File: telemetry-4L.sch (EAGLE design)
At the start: 74 parts, among them SW1 MF-SW-TACT-4.2MM, SW2 PCM12SMTR, U1 ATSAMD21G18A-MUT, U2 SPX3819M5-L-3-0, U3 MCP73831T-2ACI/OT, U4 IRLML6344TRPBF, U5 SIM868, U6 BMP280, U7 MPU-9250, U8 TPS61253YFFR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

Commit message: More fixes of overlapping components
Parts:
- X4: MPN (none) -> 104239-1430
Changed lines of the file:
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@@
 <part name="X5" library="Seeed-Connector -2016" deviceset="ANTENNA-CONN-U-FL(3P)" device="" value="U.FL-R-SMT(10)"/>
 <part name="U$9" library="MF_Aesthetics" deviceset="GND_RAIL" device=""/>
-<part name="X4" library="SimSdCombo" deviceset="MOLEX-SD+SIM-104239" device="" value="104239-1430"/>
+<part name="X4" library="SimSdCombo" deviceset="MOLEX-SD+SIM-104239" device="" value="104239-1430">
+<attribute name="MPN" value="104239-1430"/>
+</part>
 <part name="U$4" library="microbuilder" deviceset="GND" device=""/>
 <part name="+3V11" library="MF_Aesthetics" deviceset="POWER_RAIL" device="" value="3V"/>

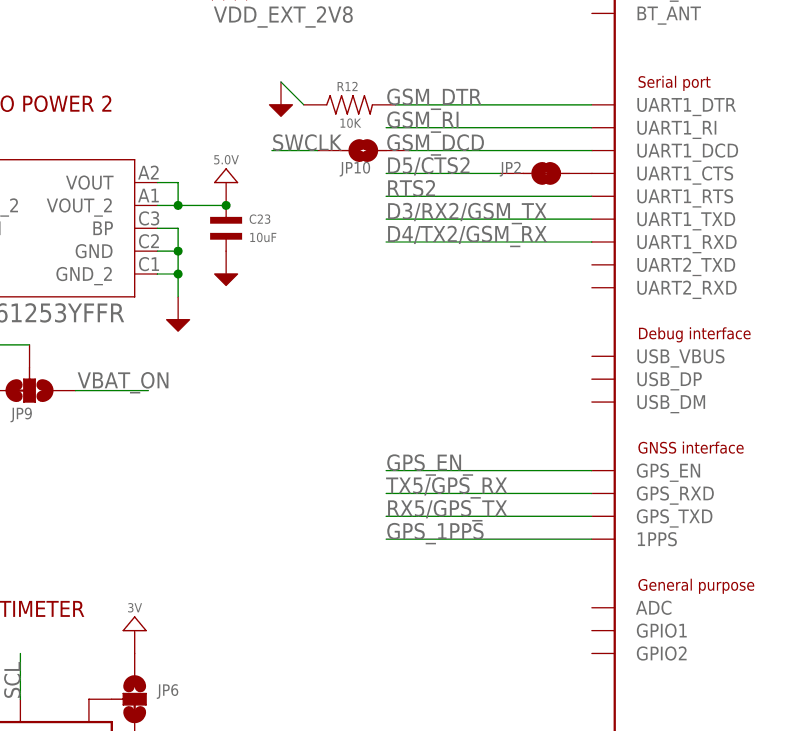
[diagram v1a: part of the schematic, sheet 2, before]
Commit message: Connected 1PPS via jumper made CTS jumper default NO
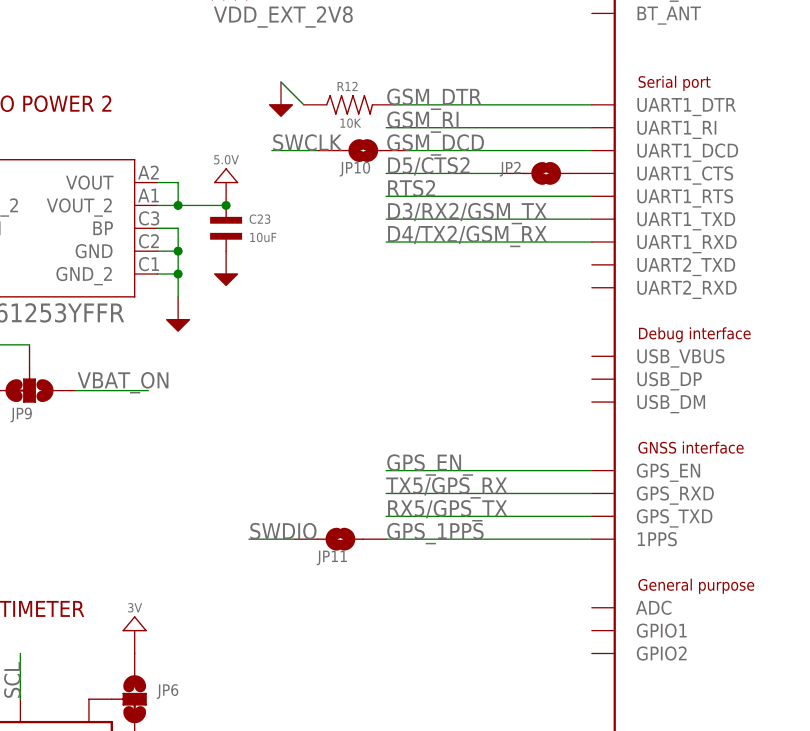
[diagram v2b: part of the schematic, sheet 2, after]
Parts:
- added JP11: JUMPER-PAD-2-NOYES_SILK, SparkFun-Passives:JUMPER-PAD-2-NOYES_SILK
- JP2: value JUMPER-PAD-2-NC_BY_TRACE -> JUMPER-PAD-2-NOYES_SILK; device SparkFun-Passives:JUMPER-PAD-2-NC_BY_TRACE -> SparkFun-Passives:JUMPER-PAD-2-NOYES_SILK
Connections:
- net GPS_1PPS: now also JP11.2
- net SWDIO: now also JP11.1
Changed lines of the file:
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@@
 <part name="U$43" library="MF_Aesthetics" deviceset="GND_RAIL" device=""/>
 <part name="U$48" library="microbuilder" deviceset="GND" device=""/>
-<part name="JP2" library="SparkFun-Passives" deviceset="JUMPER-PAD-2-NC_BY_TRACE" device="">
+<part name="JP2" library="SparkFun-Passives" deviceset="JUMPER-PAD-2-NO" device="YES_SILK">
 <attribute name="POPULATE" value="0"/>
 </part>
@@
 <part name="U$61" library="MF_Aesthetics" deviceset="GND_RAIL" device=""/>
 <part name="JP10" library="SparkFun-Passives" deviceset="JUMPER-PAD-2-NO" device="YES_SILK">
+<attribute name="POPULATE" value="0"/>
+</part>
+<part name="JP11" library="SparkFun-Passives" deviceset="JUMPER-PAD-2-NO" device="YES_SILK">
 <attribute name="POPULATE" value="0"/>
 </part>
@@
 <attribute name="NAME" x="137.16" y="114.3" size="1.27" layer="95"/>
 <attribute name="POPULATE" x="139.7" y="116.84" size="1.778" layer="96" display="off"/>
+</instance>
+<instance part="JP11" gate="G$1" x="137.16" y="73.66" smashed="yes">
+<attribute name="NAME" x="134.62" y="71.12" size="1.27" layer="95"/>
+<attribute name="POPULATE" x="137.16" y="73.66" size="1.778" layer="96" display="off"/>
 </instance>
 </instances>
@@
 <wire x1="165.1" y1="73.66" x2="142.24" y2="73.66" width="0.1524" layer="91"/>
 <label x="142.24" y="73.66" size="1.778" layer="95"/>
+<pinref part="JP11" gate="G$1" pin="2"/>
 </segment>
 </net>
@@
 </segment>
 </net>
+<net name="SWDIO" class="0">
+<segment>
+<pinref part="JP11" gate="G$1" pin="1"/>
+<wire x1="132.08" y1="73.66" x2="127" y2="73.66" width="0.1524" layer="91"/>
+<label x="127" y="73.66" size="1.778" layer="95"/>
+</segment>
+</net>

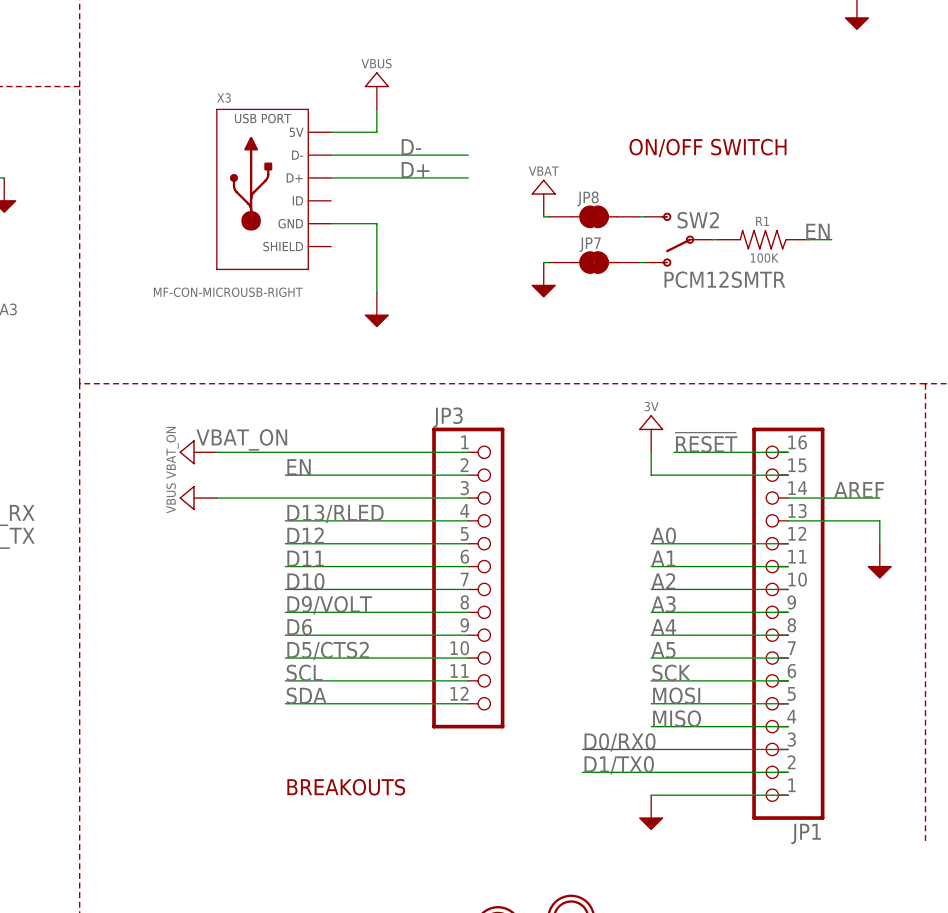
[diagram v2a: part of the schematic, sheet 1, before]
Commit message: Increased margins in middle part of board
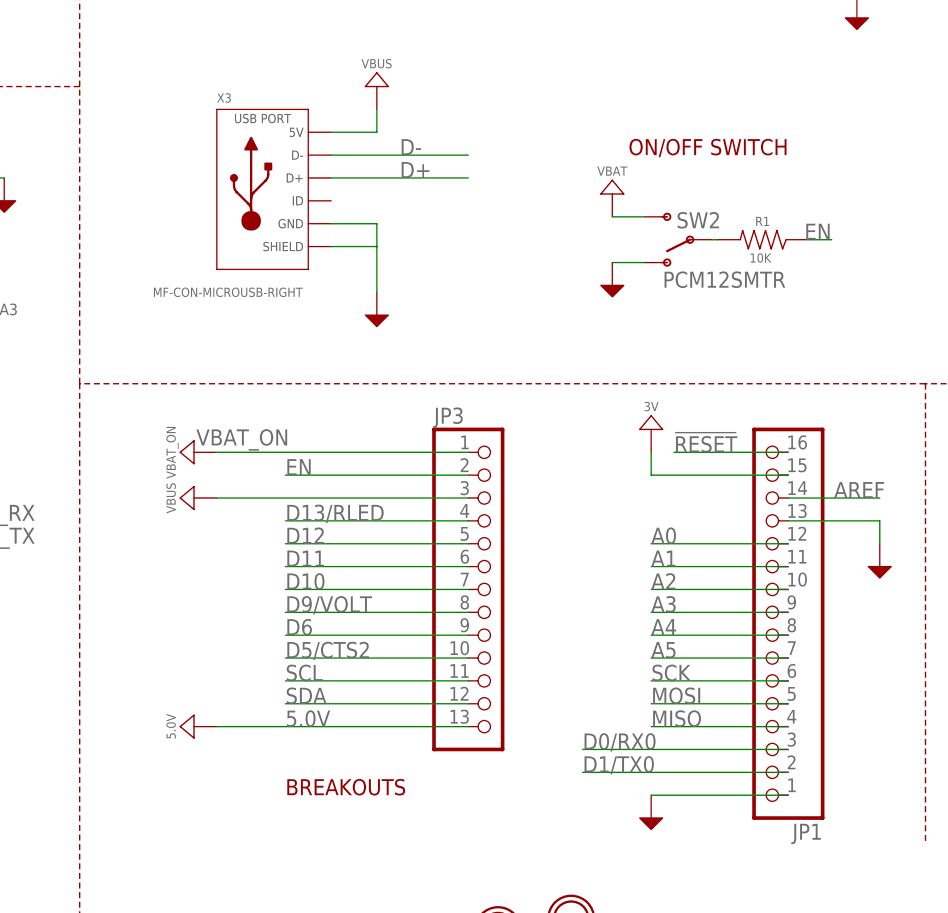
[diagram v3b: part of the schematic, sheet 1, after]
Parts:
- removed JP7, JP8: JUMPER-PAD-2-NC_BY_TRACE, SparkFun-Passives:JUMPER-PAD-2-NC_BY_TRACE
- removed X7: S2B-PH-SM4-TB(LF)(SN), microbuilder:CON_JST_PH_2PIN
- JP3: device microbuilder:HEADER-1X12 -> microbuilder:HEADER-1X13; POPULATE 0 -> (none)
- R1: value 100K -> 10K
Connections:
- removed net N$12: JP7.2, SW2.O
- removed net N$13: JP8.2, SW2.S
- net 5.0V: now also JP3.13; no longer X7.2
- net GND: now also SW2.O, X3.SLD; no longer JP7.1, X7.1
- net VBAT: now also SW2.S; no longer JP8.1
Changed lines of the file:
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@@
 <part name="U$16" library="MF_Aesthetics" deviceset="POWER_RAIL" device="" value="VBAT"/>
 <part name="U$22" library="MF_Aesthetics" deviceset="GND_RAIL" device=""/>
-<part name="JP3" library="microbuilder" deviceset="HEADER-1X12" device="">
-<attribute name="POPULATE" value="0"/>
-</part>
 <part name="U3" library="microbuilder" deviceset="MCP73831/2" device="" value="MCP73831T-2ACI/OT"/>
 <part name="U$33" library="MF_Aesthetics" deviceset="GND_RAIL" device=""/>
@@
 <part name="R8" library="MF_Passives" deviceset="RESISTOR" device="_0402" value="10K"/>
 <part name="R7" library="MF_Passives" deviceset="RESISTOR" device="_0402" value="1K"/>
-<part name="R1" library="MF_Passives" deviceset="RESISTOR" device="_0402" value="100K"/>
+<part name="R1" library="MF_Passives" deviceset="RESISTOR" device="_0402" value="10K"/>
 <part name="C1" library="MF_Passives" deviceset="CAPACITOR_NP" device="_0402" value="1uF"/>
 <part name="R4" library="MF_Passives" deviceset="RESISTOR" device="_0402" value="4.7K"/>
@@
 <part name="U$51" library="MF_Aesthetics" deviceset="GND_RAIL" device=""/>
 <part name="U$44" library="MF_Aesthetics" deviceset="POWER_RAIL" device="" value="VBAT"/>
-<part name="JP7" library="SparkFun-Passives" deviceset="JUMPER-PAD-2-NC_BY_TRACE" device="">
-<attribute name="POPULATE" value="0"/>
-</part>
-<part name="JP8" library="SparkFun-Passives" deviceset="JUMPER-PAD-2-NC_BY_TRACE" device="">
-<attribute name="POPULATE" value="0"/>
-</part>
 <part name="U4" library="MF_Discrete_Semiconductor" deviceset="N-CHANNEL_FET" device="_SOT-23-3" value="IRLML6344TRPBF"/>
 <part name="VBAT" library="MF_Aesthetics" deviceset="POWER_RAIL" device="" value="VBAT"/>
@@
 <part name="U$25" library="MF_Aesthetics" deviceset="GND_RAIL" device=""/>
 <part name="U$26" library="microbuilder" deviceset="GND" device=""/>
-<part name="X7" library="microbuilder" deviceset="CON_JST_PH_2PIN" device="" value="S2B-PH-SM4-TB(LF)(SN)"/>
 <part name="U8" library="Custom" deviceset="TPS61253YFFT" device="" value="TPS61253YFFR"/>
 <part name="L1" library="MF_Passives" deviceset="INDUCTOR" device="_1210" value="1uH">
@@
 <attribute name="POPULATE" value="0"/>
 </part>
+<part name="JP3" library="microbuilder" deviceset="HEADER-1X13" device=""/>
+<part name="5.0V" library="MF_Aesthetics" deviceset="POWER_RAIL" device="" value="5.0V"/>
 </parts>
 <sheets>
@@
 <attribute name="POPULATE" x="0" y="0" size="1.778" layer="96" display="off"/>
 </instance>
-<instance part="JP3" gate="G$1" x="180.34" y="66.04">
-<attribute name="POPULATE" x="180.34" y="66.04" size="1.778" layer="96" display="off"/>
-</instance>
 <instance part="U3" gate="G$1" x="187.96" y="144.78"/>
 <instance part="U$33" gate="G$1" x="220.98" y="129.54"/>
@@
 <instance part="U$45" gate="G$1" x="83.82" y="127"/>
 <instance part="U$47" gate="G$1" x="121.666" y="134.62"/>
-<instance part="U$49" gate="G$1" x="186.182" y="99.822"/>
+<instance part="U$49" gate="G$1" x="193.802" y="99.822"/>
 <instance part="U$50" gate="G$1" x="242.824" y="45.72"/>
 <instance part="U$51" gate="G$1" x="198.12" y="40.64"/>
-<instance part="U$44" gate="G$1" x="186.182" y="109.982"/>
-<instance part="JP7" gate="G$1" x="191.77" y="102.362" smashed="yes">
-<attribute name="NAME" x="190.246" y="103.886" size="1.27" layer="95"/>
-<attribute name="POPULATE" x="191.77" y="102.362" size="1.778" layer="96" display="off"/>
-</instance>
-<instance part="JP8" gate="G$1" x="191.77" y="107.442" smashed="yes">
-<attribute name="NAME" x="189.992" y="108.966" size="1.27" layer="95"/>
-<attribute name="POPULATE" x="191.77" y="107.442" size="1.778" layer="96" display="off"/>
-</instance>
+<instance part="U$44" gate="G$1" x="193.802" y="109.982"/>
 <instance part="U$59" gate="G$1" x="246.38" y="126.492"/>
 <instance part="U$60" gate="G$1" x="147.32" y="81.28" rot="R90"/>
+<instance part="JP3" gate="G$1" x="180.34" y="66.04"/>
+<instance part="5.0V" gate="G$1" x="147.32" y="50.8" rot="R90"/>
 </instances>
 <busses>
@@
 </segment>
 <segment>
-<wire x1="167.64" y1="106.68" x2="167.64" y2="99.06" width="0.1524" layer="91"/>
+<wire x1="167.64" y1="106.68" x2="167.64" y2="104.14" width="0.1524" layer="91"/>
 <pinref part="X3" gate="G$1" pin="GND"/>
+<wire x1="167.64" y1="104.14" x2="167.64" y2="99.06" width="0.1524" layer="91"/>
 <wire x1="167.64" y1="106.68" x2="162.56" y2="106.68" width="0.1524" layer="91"/>
 <pinref part="U$18" gate="G$1" pin="P$1"/>
+<wire x1="162.56" y1="104.14" x2="167.64" y2="104.14" width="0.1524" layer="91"/>
+<pinref part="X3" gate="G$1" pin="SLD"/>
 </segment>
 <segment>
@@
 </segment>
 <segment>
-<pinref part="JP7" gate="G$1" pin="1"/>
 <pinref part="U$49" gate="G$1" pin="P$1"/>
-<wire x1="186.182" y1="102.362" x2="186.69" y2="102.362" width="0.1524" layer="91"/>
+<wire x1="193.802" y1="102.362" x2="197.358" y2="102.362" width="0.1524" layer="91"/>
+<pinref part="SW2" gate="G$1" pin="O"/>
 </segment>
 </net>
@@
 <segment>
 <pinref part="U$44" gate="G$1" pin="P$1"/>
-<pinref part="JP8" gate="G$1" pin="1"/>
-<wire x1="186.69" y1="107.442" x2="186.182" y2="107.442" width="0.1524" layer="91"/>
+<pinref part="SW2" gate="G$1" pin="S"/>
+<wire x1="193.802" y1="107.442" x2="197.358" y2="107.442" width="0.1524" layer="91"/>
 </segment>
 </net>
@@
 <segment>
 <wire x1="157.48" y1="78.74" x2="177.8" y2="78.74" width="0.1524" layer="91"/>
+<label x="157.48" y="78.74" size="1.778" layer="95"/>
 <pinref part="JP3" gate="G$1" pin="2"/>
-<label x="157.48" y="78.74" size="1.778" layer="95"/>
 </segment>
 <segment>
@@
 <pinref part="R1" gate="G$1" pin="P$2"/>
 <wire x1="205.486" y1="104.902" x2="204.978" y2="104.902" width="0.1524" layer="91"/>
-</segment>
-</net>
-<net name="N$12" class="0">
-<segment>
-<pinref part="SW2" gate="G$1" pin="O"/>
-<pinref part="JP7" gate="G$1" pin="2"/>
-<wire x1="196.85" y1="102.362" x2="197.358" y2="102.362" width="0.1524" layer="91"/>
-</segment>
-</net>
-<net name="N$13" class="0">
-<segment>
-<pinref part="SW2" gate="G$1" pin="S"/>
-<pinref part="JP8" gate="G$1" pin="2"/>
-<wire x1="196.85" y1="107.442" x2="197.358" y2="107.442" width="0.1524" layer="91"/>
 </segment>
 </net>
@@
 <segment>
 <wire x1="149.86" y1="81.28" x2="177.8" y2="81.28" width="0.1524" layer="91"/>
-<pinref part="JP3" gate="G$1" pin="1"/>
 <label x="147.574" y="82.042" size="1.778" layer="95"/>
 <pinref part="U$60" gate="G$1" pin="P$1"/>
+<pinref part="JP3" gate="G$1" pin="1"/>
 </segment>
 </net>
@@
 <wire x1="104.14" y1="22.86" x2="119.38" y2="22.86" width="0.1524" layer="91"/>
 <label x="111.76" y="22.86" size="1.778" layer="95"/>
+</segment>
+</net>
+<net name="5.0V" class="0">
+<segment>
+<pinref part="JP3" gate="G$1" pin="13"/>
+<wire x1="177.8" y1="50.8" x2="149.86" y2="50.8" width="0.1524" layer="91"/>
+<label x="157.48" y="50.8" size="1.778" layer="95"/>
+<pinref part="5.0V" gate="G$1" pin="P$1"/>
 </segment>
 </net>
@@
 <instance part="U$25" gate="G$1" x="8.636" y="22.86"/>
 <instance part="U$26" gate="G$1" x="19.05" y="40.64"/>
-<instance part="X7" gate="G$1" x="77.724" y="147.574" smashed="yes" rot="R180">
-<attribute name="NAME" x="79.756" y="154.051" size="1.778" layer="95" rot="R180"/>
-<attribute name="VALUE" x="73.914" y="157.226" size="1.27" layer="96" rot="R270"/>
-</instance>
 <instance part="U8" gate="A" x="101.6" y="108.204"/>
 <instance part="L1" gate="G$1" x="86.106" y="113.284" smashed="yes" rot="R90">
@@
 </segment>
 <segment>
-<pinref part="X7" gate="G$1" pin="1"/>
-<wire x1="80.264" y1="145.034" x2="80.264" y2="138.176" width="0.1524" layer="91"/>
 <pinref part="U$55" gate="G$1" pin="P$1"/>
 <pinref part="C24" gate="G$1" pin="P$2"/>
 <wire x1="88.9" y1="144.78" x2="88.9" y2="138.176" width="0.1524" layer="91"/>
 <wire x1="88.9" y1="138.176" x2="80.264" y2="138.176" width="0.1524" layer="91"/>
-<junction x="80.264" y="138.176"/>
 <pinref part="R11" gate="G$1" pin="P$2"/>
 <wire x1="94.742" y1="142.24" x2="94.742" y2="138.176" width="0.1524" layer="91"/>
@@
 </segment>
 <segment>
-<pinref part="X7" gate="G$1" pin="2"/>
-<wire x1="80.264" y1="147.574" x2="80.264" y2="154.686" width="0.1524" layer="91"/>
 <pinref part="5.0V_1" gate="G$1" pin="P$1"/>
 <pinref part="C24" gate="G$1" pin="P$1"/>
 <wire x1="88.9" y1="149.86" x2="88.9" y2="154.686" width="0.1524" layer="91"/>
 <wire x1="88.9" y1="154.686" x2="80.264" y2="154.686" width="0.1524" layer="91"/>
-<junction x="80.264" y="154.686"/>
 <pinref part="R11" gate="G$1" pin="P$1"/>
 <wire x1="94.742" y1="152.4" x2="94.742" y2="154.686" width="0.1524" layer="91"/>
